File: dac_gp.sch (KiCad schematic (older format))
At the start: 7 parts, among them U10 TMUX6136PWR, U11 TMUX6136PWR, U5 DAC80508ZRTER

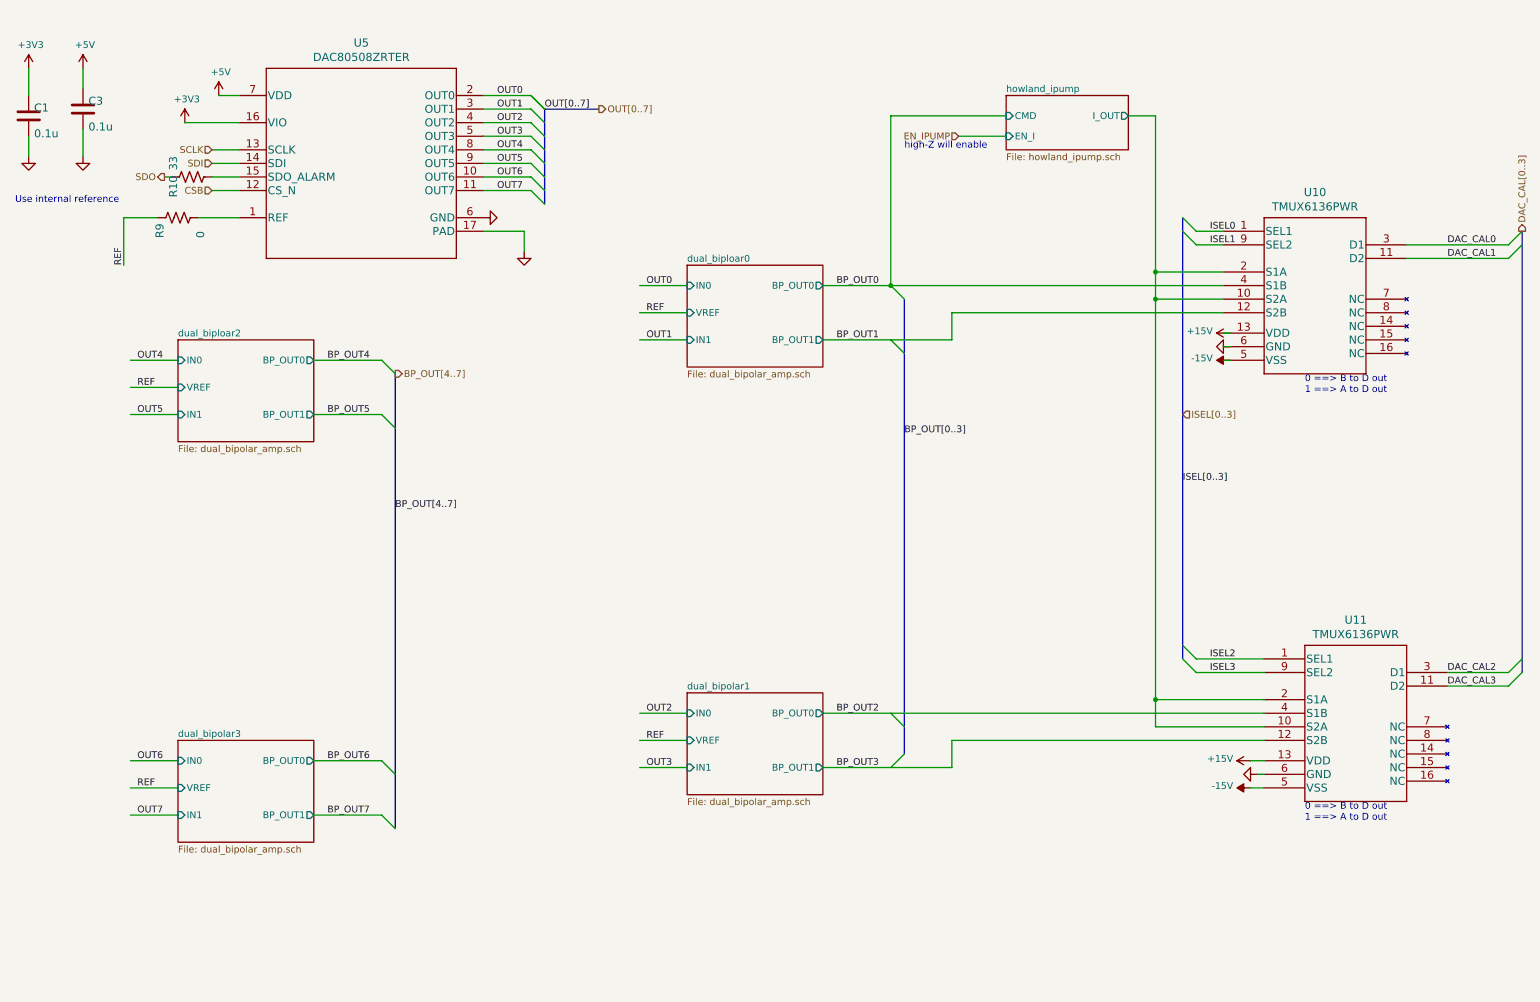
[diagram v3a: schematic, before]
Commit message: finished parts placement; reconnecting pins for less spagheti
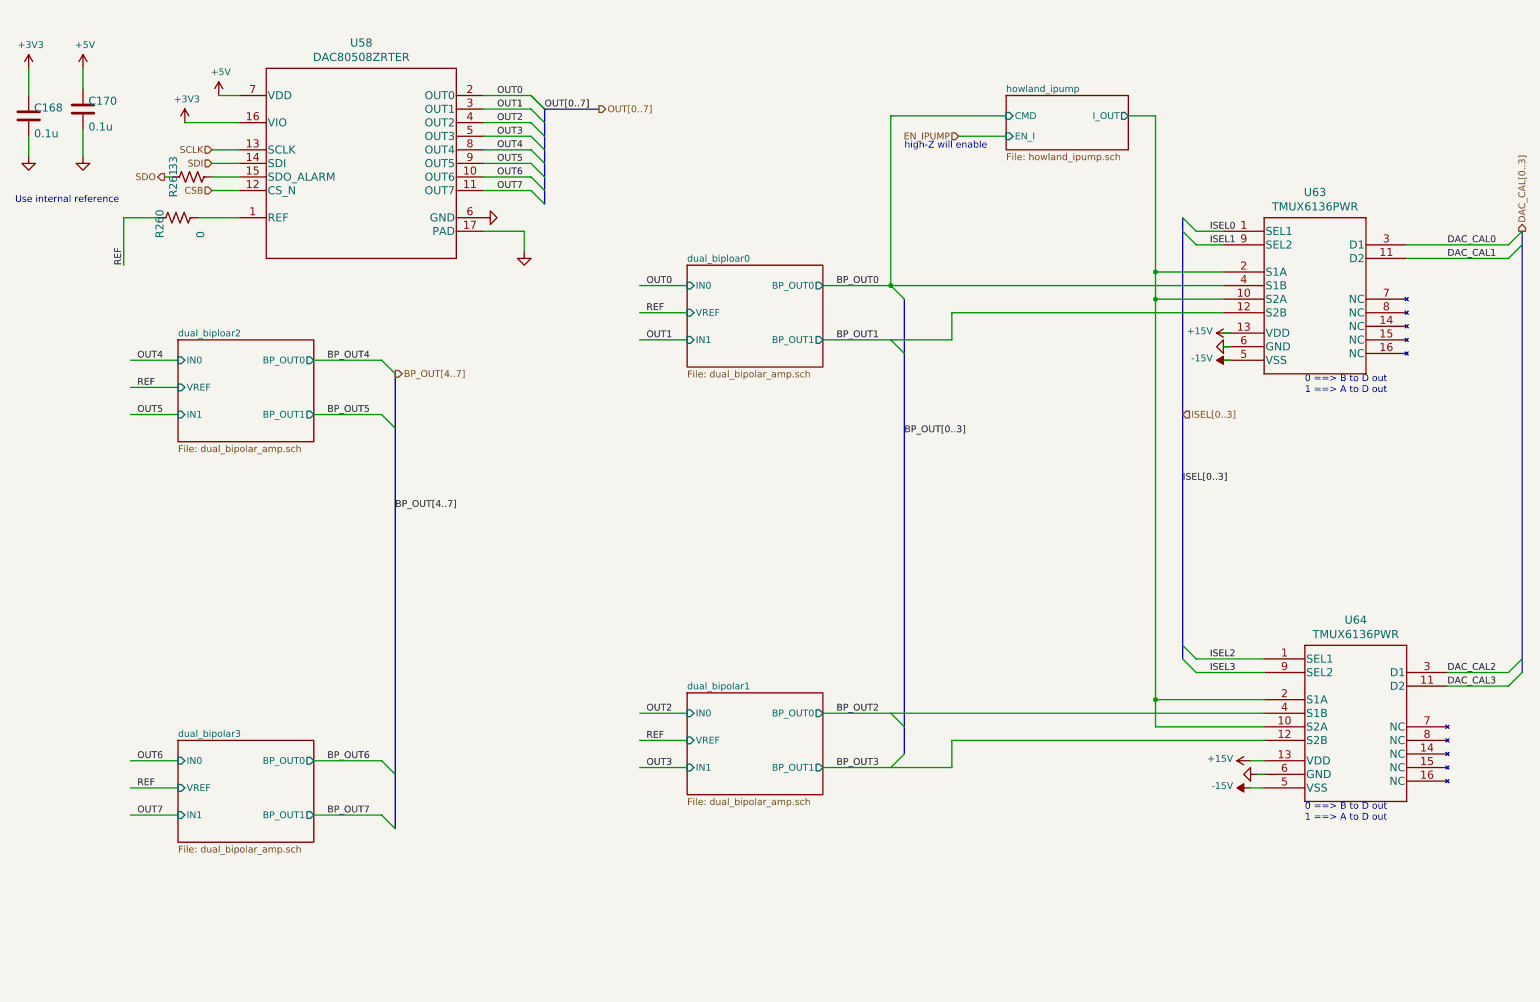
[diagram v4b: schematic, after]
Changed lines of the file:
@@
 $Descr User 12505 8268
 encoding utf-8
-Sheet 2 26
+Sheet 21 26
 Title ""
 Date ""
@@
 AR Path="/6095BD4C/519C2D15" Ref="#FRAME1"  Part="1"
 AR Path="/61B02572/519C2D15" Ref="#FRAME2"  Part="1"
-F 0 "#FRAME1" H 900 6900 50  0001 C CNN
+F 0 "#FRAME2" H 900 6900 50  0001 C CNN
 F 1 "FRAME_A_L" H 900 6900 50  0001 C CNN
 F 2 "" H 900 6900 50  0001 C CNN
@@
 AR Path="/6095BD4C/E9B71633" Ref="#GND012"  Part="1"
 AR Path="/61B02572/E9B71633" Ref="#GND0255"  Part="1"
-F 0 "#GND012" H 4300 2250 50  0001 C CNN
+F 0 "#GND0255" H 4300 2250 50  0001 C CNN
 F 1 "GND" H 4200 2150 59  0001 L BNN
 F 2 "" H 4300 2250 50  0001 C CNN
@@
 AR Path="/6095BD4C/A7A1DCDA" Ref="C1"  Part="1"
 AR Path="/61B02572/A7A1DCDA" Ref="C168"  Part="1"
-F 0 "C1" H 690 1275 59  0000 L BNN
+F 0 "C168" H 690 1275 59  0000 L BNN
 F 1 "0.1u" H 690 1085 59  0000 L BNN
 F 2 "Capacitor_SMD:C_0603_1608Metric" H 650 1250 50  0001 C CNN
@@
 AR Path="/6095BD4C/46ACB443" Ref="C3"  Part="1"
 AR Path="/61B02572/46ACB443" Ref="C170"  Part="1"
-F 0 "C3" H 1090 1225 59  0000 L BNN
+F 0 "C170" H 1090 1225 59  0000 L BNN
 F 1 "0.1u" H 1090 1035 59  0000 L BNN
 F 2 "Capacitor_SMD:C_0603_1608Metric" H 1050 1200 50  0001 C CNN
@@
 AR Path="/6095BD4C/FC55E54D" Ref="#GND01"  Part="1"
 AR Path="/61B02572/FC55E54D" Ref="#GND0244"  Part="1"
-F 0 "#GND01" H 650 1550 50  0001 C CNN
+F 0 "#GND0244" H 650 1550 50  0001 C CNN
 F 1 "GND" H 550 1450 59  0001 L BNN
 F 2 "" H 650 1550 50  0001 C CNN
@@
 AR Path="/6095BD4C/10B103BF" Ref="#GND03"  Part="1"
 AR Path="/61B02572/10B103BF" Ref="#GND0246"  Part="1"
-F 0 "#GND03" H 1050 1550 50  0001 C CNN
+F 0 "#GND0246" H 1050 1550 50  0001 C CNN
 F 1 "GND" H 950 1450 59  0001 L BNN
 F 2 "" H 1050 1550 50  0001 C CNN
@@
 AR Path="/6095BD4C/61889133" Ref="#PWR037"  Part="1"
 AR Path="/61B02572/61889133" Ref="#PWR0232"  Part="1"
-F 0 "#PWR037" H 1050 750 50  0001 C CNN
+F 0 "#PWR0232" H 1050 750 50  0001 C CNN
 F 1 "+5V" H 1065 1073 50  0000 C CNN
 F 2 "" H 1050 900 50  0001 C CNN
@@
 AR Path="/6095BD4C/6188B164" Ref="#PWR033"  Part="1"
 AR Path="/61B02572/6188B164" Ref="#PWR0228"  Part="1"
-F 0 "#PWR033" H 650 750 50  0001 C CNN
+F 0 "#PWR0228" H 650 750 50  0001 C CNN
 F 1 "+3V3" H 665 1073 50  0000 C CNN
 F 2 "" H 650 900 50  0001 C CNN
@@
 AR Path="/6095BD4C/60A11E5A" Ref="U5"  Part="1"
 AR Path="/61B02572/60A11E5A" Ref="U58"  Part="1"
-F 0 "U5" H 3100 2488 60  0000 C CNN
+F 0 "U58" H 3100 2488 60  0000 C CNN
 F 1 "DAC80508ZRTER" H 3100 2382 60  0000 C CNN
 F 2 "Package_DFN_QFN:WQFN-16-1EP_3x3mm_P0.5mm_EP1.6x1.6mm" H 3100 1540 60  0001 C CNN
@@
 AR Path="/6095BD4C/60A13242" Ref="#PWR039"  Part="1"
 AR Path="/61B02572/60A13242" Ref="#PWR0234"  Part="1"
-F 0 "#PWR039" H 1800 1150 50  0001 C CNN
+F 0 "#PWR0234" H 1800 1150 50  0001 C CNN
 F 1 "+3V3" H 1815 1473 50  0000 C CNN
 F 2 "" H 1800 1300 50  0001 C CNN
@@
 AR Path="/6095BD4C/60A13FF9" Ref="#PWR042"  Part="1"
 AR Path="/61B02572/60A13FF9" Ref="#PWR0237"  Part="1"
-F 0 "#PWR042" H 2050 950 50  0001 C CNN
+F 0 "#PWR0237" H 2050 950 50  0001 C CNN
 F 1 "+5V" H 2065 1273 50  0000 C CNN
 F 2 "" H 2050 1100 50  0001 C CNN
@@
 AR Path="/6095BD4C/60A174FD" Ref="#GND011"  Part="1"
 AR Path="/61B02572/60A174FD" Ref="#GND0254"  Part="1"
-F 0 "#GND011" H 4000 2000 50  0001 C CNN
+F 0 "#GND0254" H 4000 2000 50  0001 C CNN
 F 1 "GND" H 3900 1900 59  0001 L BNN
 F 2 "" H 4000 2000 50  0001 C CNN
@@
 AR Path="/6095BD4C/60A29EE1" Ref="R9"  Part="1"
 AR Path="/61B02572/60A29EE1" Ref="R260"  Part="1"
-F 0 "R9" H 1600 2100 59  0000 L BNN
+F 0 "R260" H 1600 2100 59  0000 L BNN
 F 1 "0" H 1600 1800 59  0000 L BNN
 F 2 "Resistor_SMD:R_0603_1608Metric" H 1750 2000 50  0001 C CNN
@@
 AR Path="/6095BD4C/60B8C0FB" Ref="U10"  Part="1"
 AR Path="/61B02572/60B8C0FB" Ref="U63"  Part="1"
-F 0 "U10" H 10125 2387 60  0000 C CNN
+F 0 "U63" H 10125 2387 60  0000 C CNN
 F 1 "TMUX6136PWR" H 10125 2281 60  0000 C CNN
 F 2 "Package_SO:TSSOP-16_4.4x5mm_P0.65mm" H 10100 2200 60  0001 C CNN
@@
 AR Path="/6095BD4C/60BE8CAA" Ref="#PWR053"  Part="1"
 AR Path="/61B02572/60BE8CAA" Ref="#PWR0248"  Part="1"
-F 0 "#PWR053" H 9500 2700 50  0001 C CNN
+F 0 "#PWR0248" H 9500 2700 50  0001 C CNN
 F 1 "+15V" V 9515 2978 50  0000 L CNN
 F 2 "" H 9500 2850 50  0001 C CNN
@@
 AR Path="/6095BD4C/60BEA680" Ref="#PWR054"  Part="1"
 AR Path="/61B02572/60BEA680" Ref="#PWR0249"  Part="1"
-F 0 "#PWR054" H 9500 3150 50  0001 C CNN
+F 0 "#PWR0249" H 9500 3150 50  0001 C CNN
 F 1 "-15V" V 9515 3178 50  0000 L CNN
 F 2 "" H 9500 3050 50  0001 C CNN
@@
 AR Path="/6095BD4C/60BEBA41" Ref="#GND021"  Part="1"
 AR Path="/61B02572/60BEBA41" Ref="#GND0264"  Part="1"
-F 0 "#GND021" H 9500 2950 50  0001 C CNN
+F 0 "#GND0264" H 9500 2950 50  0001 C CNN
 F 1 "GND" H 9400 2850 59  0001 L BNN
 F 2 "" H 9500 2950 50  0001 C CNN
@@
 AR Path="/6095BD4C/60C5A3EA" Ref="U11"  Part="1"
 AR Path="/61B02572/60C5A3EA" Ref="U64"  Part="1"
-F 0 "U11" H 10425 5537 60  0000 C CNN
+F 0 "U64" H 10425 5537 60  0000 C CNN
 F 1 "TMUX6136PWR" H 10425 5431 60  0000 C CNN
 F 2 "Package_SO:TSSOP-16_4.4x5mm_P0.65mm" H 10400 5350 60  0001 C CNN
@@
 AR Path="/6095BD4C/60C5A432" Ref="#PWR055"  Part="1"
 AR Path="/61B02572/60C5A432" Ref="#PWR0250"  Part="1"
-F 0 "#PWR055" H 9650 5850 50  0001 C CNN
+F 0 "#PWR0250" H 9650 5850 50  0001 C CNN
 F 1 "+15V" V 9665 6128 50  0000 L CNN
 F 2 "" H 9650 6000 50  0001 C CNN
@@
 AR Path="/6095BD4C/60C5A439" Ref="#PWR056"  Part="1"
 AR Path="/61B02572/60C5A439" Ref="#PWR0251"  Part="1"
-F 0 "#PWR056" H 9650 6300 50  0001 C CNN
+F 0 "#PWR0251" H 9650 6300 50  0001 C CNN
 F 1 "-15V" V 9665 6328 50  0000 L CNN
 F 2 "" H 9650 6200 50  0001 C CNN
@@
 AR Path="/6095BD4C/60C5A440" Ref="#GND022"  Part="1"
 AR Path="/61B02572/60C5A440" Ref="#GND0265"  Part="1"
-F 0 "#GND022" H 9700 6100 50  0001 C CNN
+F 0 "#GND0265" H 9700 6100 50  0001 C CNN
 F 1 "GND" H 9600 6000 59  0001 L BNN
 F 2 "" H 9700 6100 50  0001 C CNN
@@
 AR Path="/6095BD4C/617C87E1" Ref="R10"  Part="1"
 AR Path="/61B02572/617C87E1" Ref="R261"  Part="1"
-F 0 "R10" H 1700 1800 59  0000 L BNN
+F 0 "R261" H 1700 1800 59  0000 L BNN
 F 1 "33" H 1900 1800 59  0000 L BNN
 F 2 "Resistor_SMD:R_0603_1608Metric" H 1850 1700 50  0001 C CNN

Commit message: moved adc pins around
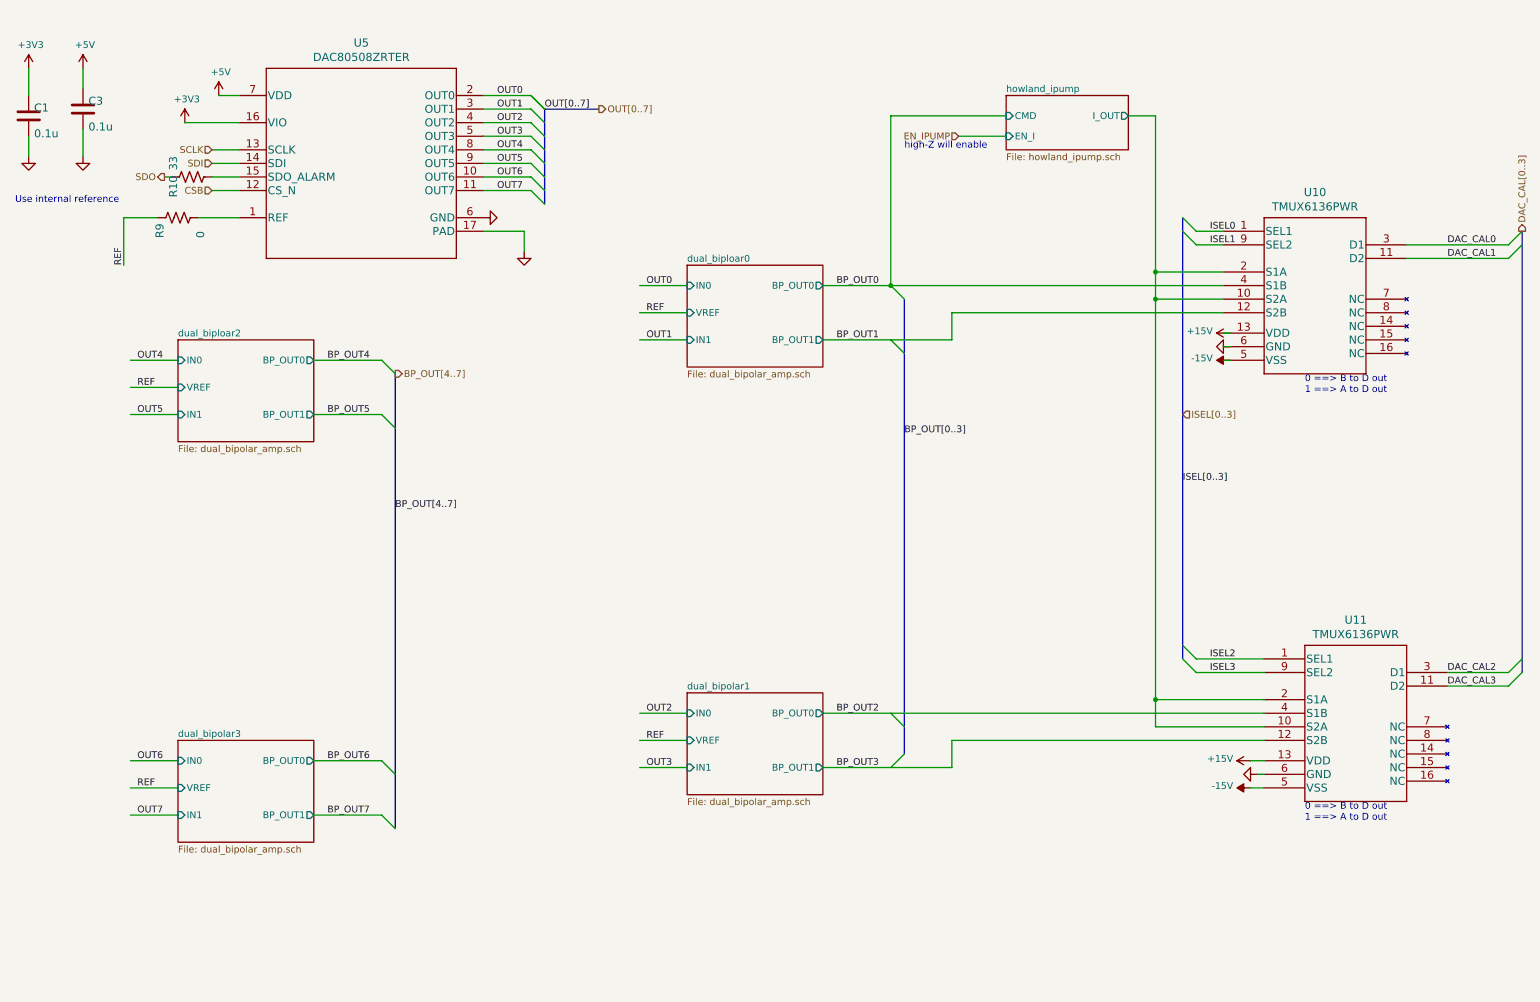
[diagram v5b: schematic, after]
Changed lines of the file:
@@
 $Descr User 12505 8268
 encoding utf-8
-Sheet 21 26
+Sheet 2 26
 Title ""
 Date ""
@@
 AR Path="/6095BD4C/519C2D15" Ref="#FRAME1"  Part="1"
 AR Path="/61B02572/519C2D15" Ref="#FRAME2"  Part="1"
-F 0 "#FRAME2" H 900 6900 50  0001 C CNN
+F 0 "#FRAME1" H 900 6900 50  0001 C CNN
 F 1 "FRAME_A_L" H 900 6900 50  0001 C CNN
 F 2 "" H 900 6900 50  0001 C CNN
@@
 AR Path="/6095BD4C/A7A1DCDA" Ref="C1"  Part="1"
 AR Path="/61B02572/A7A1DCDA" Ref="C168"  Part="1"
-F 0 "C168" H 690 1275 59  0000 L BNN
+F 0 "C1" H 690 1275 59  0000 L BNN
 F 1 "0.1u" H 690 1085 59  0000 L BNN
 F 2 "Capacitor_SMD:C_0603_1608Metric" H 650 1250 50  0001 C CNN
@@
 AR Path="/6095BD4C/46ACB443" Ref="C3"  Part="1"
 AR Path="/61B02572/46ACB443" Ref="C170"  Part="1"
-F 0 "C170" H 1090 1225 59  0000 L BNN
+F 0 "C3" H 1090 1225 59  0000 L BNN
 F 1 "0.1u" H 1090 1035 59  0000 L BNN
 F 2 "Capacitor_SMD:C_0603_1608Metric" H 1050 1200 50  0001 C CNN
@@
 AR Path="/6095BD4C/60A11E5A" Ref="U5"  Part="1"
 AR Path="/61B02572/60A11E5A" Ref="U58"  Part="1"
-F 0 "U58" H 3100 2488 60  0000 C CNN
+F 0 "U5" H 3100 2488 60  0000 C CNN
 F 1 "DAC80508ZRTER" H 3100 2382 60  0000 C CNN
 F 2 "Package_DFN_QFN:WQFN-16-1EP_3x3mm_P0.5mm_EP1.6x1.6mm" H 3100 1540 60  0001 C CNN
@@
 AR Path="/6095BD4C/60A29EE1" Ref="R9"  Part="1"
 AR Path="/61B02572/60A29EE1" Ref="R260"  Part="1"
-F 0 "R260" H 1600 2100 59  0000 L BNN
+F 0 "R9" H 1600 2100 59  0000 L BNN
 F 1 "0" H 1600 1800 59  0000 L BNN
 F 2 "Resistor_SMD:R_0603_1608Metric" H 1750 2000 50  0001 C CNN
@@
 AR Path="/6095BD4C/60B8C0FB" Ref="U10"  Part="1"
 AR Path="/61B02572/60B8C0FB" Ref="U63"  Part="1"
-F 0 "U63" H 10125 2387 60  0000 C CNN
+F 0 "U10" H 10125 2387 60  0000 C CNN
 F 1 "TMUX6136PWR" H 10125 2281 60  0000 C CNN
 F 2 "Package_SO:TSSOP-16_4.4x5mm_P0.65mm" H 10100 2200 60  0001 C CNN
@@
 AR Path="/6095BD4C/60C5A3EA" Ref="U11"  Part="1"
 AR Path="/61B02572/60C5A3EA" Ref="U64"  Part="1"
-F 0 "U64" H 10425 5537 60  0000 C CNN
+F 0 "U11" H 10425 5537 60  0000 C CNN
 F 1 "TMUX6136PWR" H 10425 5431 60  0000 C CNN
 F 2 "Package_SO:TSSOP-16_4.4x5mm_P0.65mm" H 10400 5350 60  0001 C CNN
@@
 AR Path="/6095BD4C/617C87E1" Ref="R10"  Part="1"
 AR Path="/61B02572/617C87E1" Ref="R261"  Part="1"
-F 0 "R261" H 1700 1800 59  0000 L BNN
+F 0 "R10" H 1700 1800 59  0000 L BNN
 F 1 "33" H 1900 1800 59  0000 L BNN
 F 2 "Resistor_SMD:R_0603_1608Metric" H 1850 1700 50  0001 C CNN
